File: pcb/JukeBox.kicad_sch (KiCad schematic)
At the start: 99 parts, among them J1 USB_C_Receptacle_USB2.0_16P, Q1 Q_NPN_BEC, SW1 SW_SPST, SW10 SW_SPST, SW11 SW_SPST, SW12 SW_SPST, SW2 SW_SPST, SW3 SW_SPST, SW4 SW_SPST, SW5 SW_SPST, SW6 SW_SPST, SW7 SW_SPST, SW8 SW_SPST, SW9 SW_SPST, U1 NCP1117-3.3_SOT223, U2 W25Q128JVS, U3 RP2350_60QFN, U5 CAT24C512, Y2 ABM8-272-T3

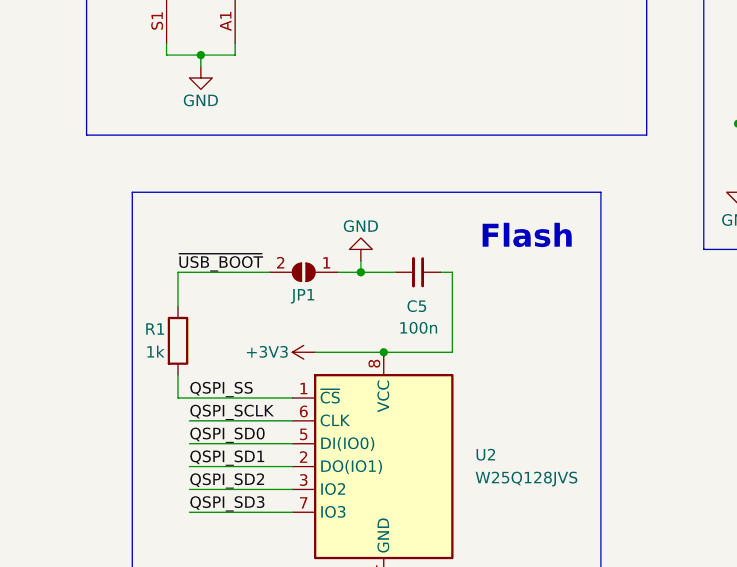
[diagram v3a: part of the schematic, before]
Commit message: add bootsel button instead of pad
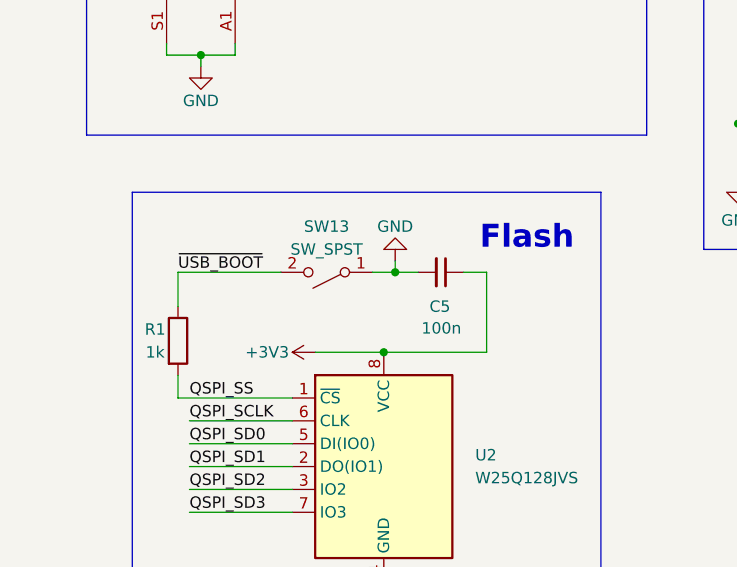
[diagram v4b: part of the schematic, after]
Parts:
- removed JP1: SolderJumper_2_Open, Jumper:SolderJumper-2_P1.3mm_Open_RoundedPad1.0x1.5mm, symbol Jumper:SolderJumper_2_Open
- added SW13: SW_SPST, Button_Switch_SMD:SW_SPST_CK_RS282G05A3, symbol Switch:SW_SPST
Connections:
- net GND: now also SW13.1 (A)
- net ~{USB_BOOT}: now also SW13.2 (B)
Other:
- moved on the sheet: C5
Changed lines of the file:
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@@
 	)
 	(junction
+		(at 58.42 99.06)
+		(diameter 0)
+		(color 0 0 0 0)
+	)
+	(junction
 		(at 111.76 82.55)
 		(diameter 0)
@@
 	)
 	(junction
-		(at 54.61 99.06)
-		(diameter 0)
-		(color 0 0 0 0)
-	)
-	(junction
 		(at 360.68 231.14)
 		(diameter 0)
@@
 	(wire
 		(pts
+			(xy 58.42 99.06) (xy 60.96 99.06)
+		)
+		(stroke
+			(width 0)
+			(type default)
+		)
+	)
+	(wire
+		(pts
 			(xy 203.2 157.48) (xy 203.2 158.75)
 		)
@@
 	(wire
 		(pts
-			(xy 57.15 107.95) (xy 64.77 107.95)
+			(xy 57.15 107.95) (xy 68.58 107.95)
 		)
 		(stroke
@@
 	(wire
 		(pts
-			(xy 63.5 99.06) (xy 64.77 99.06)
+			(xy 66.04 99.06) (xy 68.58 99.06)
 		)
 		(stroke
@@
 	(wire
 		(pts
-			(xy 54.61 97.79) (xy 54.61 99.06)
+			(xy 58.42 97.79) (xy 58.42 99.06)
+		)
+		(stroke
+			(width 0)
+			(type default)
+		)
+	)
+	(wire
+		(pts
+			(xy 55.88 99.06) (xy 58.42 99.06)
 		)
 		(stroke
@@
 	(wire
 		(pts
-			(xy 64.77 99.06) (xy 64.77 107.95)
+			(xy 68.58 99.06) (xy 68.58 107.95)
 		)
 		(stroke
@@
 	(wire
 		(pts
-			(xy 54.61 99.06) (xy 58.42 99.06)
-		)
-		(stroke
-			(width 0)
-			(type default)
-		)
-	)
-	(wire
-		(pts
 			(xy 173.99 157.48) (xy 171.45 157.48)
 		)
@@
 	(wire
 		(pts
-			(xy 34.29 99.06) (xy 44.45 99.06)
+			(xy 34.29 99.06) (xy 45.72 99.06)
 		)
 		(stroke
@@
 	(wire
 		(pts
-			(xy 52.07 99.06) (xy 54.61 99.06)
-		)
-		(stroke
-			(width 0)
-			(type default)
-		)
-	)
-	(wire
-		(pts
 			(xy 171.45 135.89) (xy 171.45 137.16)
 		)
@@
 	(symbol
 		(lib_id "Device:C_Small")
-		(at 60.96 99.06 270)
+		(at 63.5 99.06 270)
 		(unit 1)
 		(exclude_from_sim no)
@@
 		(dnp no)
 		(property "Reference" "C5"
-			(at 59.69 102.87 90)
+			(at 62.23 102.87 90)
 			(effects
 				(font
@@
 		)
 		(property "Value" "100n"
-			(at 58.801 105.283 90)
+			(at 61.341 105.283 90)
 			(effects
 				(font
@@
 		)
 		(property "Footprint" "Capacitor_SMD:C_0402_1005Metric"
-			(at 60.96 99.06 0)
+			(at 63.5 99.06 0)
 			(effects
 				(font
@@
 		)
 		(property "Datasheet" "~"
-			(at 60.96 99.06 0)
+			(at 63.5 99.06 0)
 			(effects
 				(font
@@
 		)
 		(property "Description" "Unpolarized capacitor, small symbol"
-			(at 60.96 99.06 0)
+			(at 63.5 99.06 0)
 			(effects
 				(font
@@
 	)
 	(symbol
-		(lib_id "Jumper:SolderJumper_2_Open")
-		(at 48.26 99.06 180)
-		(unit 1)
-		(exclude_from_sim no)
-		(in_bom yes)
-		(on_board yes)
-		(dnp no)
-		(property "Reference" "JP1"
-			(at 48.26 101.6 0)
-			(effects
-				(font
-					(size 1.27 1.27)
-				)
-			)
-		)
-		(property "Value" "SolderJumper_2_Open"
-			(at 48.26 104.14 0)
-			(effects
-				(font
-					(size 1.27 1.27)
-				)
-				(hide yes)
-			)
-		)
-		(property "Footprint" "Jumper:SolderJumper-2_P1.3mm_Open_RoundedPad1.0x1.5mm"
-			(at 48.26 99.06 0)
-			(effects
-				(font
-					(size 1.27 1.27)
-				)
-				(hide yes)
-			)
-		)
-		(property "Datasheet" "~"
-			(at 48.26 99.06 0)
-			(effects
-				(font
-					(size 1.27 1.27)
-				)
-				(hide yes)
-			)
-		)
-		(property "Description" ""
-			(at 48.26 99.06 0)
-			(effects
-				(font
-					(size 1.27 1.27)
-				)
-				(hide yes)
-			)
-		)
-		(pin "1"
-		)
-		(pin "2"
-		)
-		(instances
-			(project "JukeBox"
-				(path "/6328db6d-b3ae-4344-8bbe-195d6ec45eb3"
-					(reference "JP1")
-					(unit 1)
-				)
-			)
-		)
-	)
-	(symbol
 		(lib_id "Device:R")
 		(at 360.68 204.47 0)
@@
 	(symbol
 		(lib_id "power:GND")
-		(at 54.61 97.79 180)
+		(at 58.42 97.79 180)
 		(unit 1)
 		(exclude_from_sim no)
@@
 		(dnp no)
 		(property "Reference" "#PWR022"
-			(at 54.61 91.44 0)
+			(at 58.42 91.44 0)
 			(effects
 				(font
@@
 		)
 		(property "Value" "GND"
-			(at 54.61 93.98 0)
+			(at 58.42 93.98 0)
 			(effects
 				(font
@@
 		)
 		(property "Footprint" ""
-			(at 54.61 97.79 0)
+			(at 58.42 97.79 0)
 			(effects
 				(font
@@
 		)
 		(property "Datasheet" ""
-			(at 54.61 97.79 0)
+			(at 58.42 97.79 0)
 			(effects
 				(font
@@
 		)
 		(property "Description" ""
-			(at 54.61 97.79 0)
+			(at 58.42 97.79 0)
 			(effects
 				(font
@@
 					(unit 1)
 				)
+			)
+		)
+	)
+	(symbol
+		(lib_id "Switch:SW_SPST")
+		(at 50.8 99.06 180)
+		(unit 1)
+		(exclude_from_sim no)
+		(in_bom yes)
+		(on_board yes)
+		(dnp no)
+		(fields_autoplaced yes)
+		(property "Reference" "SW13"
+			(at 50.8 93.98 0)
+			(effects
+				(font
+					(size 1.27 1.27)
+				)
+			)
+		)
+		(property "Value" "SW_SPST"
+			(at 50.8 96.52 0)
+			(effects
+				(font
+					(size 1.27 1.27)
+				)
+			)
+		)
+		(property "Footprint" "Button_Switch_SMD:SW_SPST_CK_RS282G05A3"
+			(at 50.8 99.06 0)
+			(effects
+				(font
+					(size 1.27 1.27)
+				)
+				(hide yes)
+			)
+		)
+		(property "Datasheet" "~"
+			(at 50.8 99.06 0)
+			(effects
+				(font
+					(size 1.27 1.27)
+				)
+				(hide yes)
+			)
+		)
+		(property "Description" "Single Pole Single Throw (SPST) switch"
+			(at 50.8 99.06 0)
+			(effects
+				(font
+					(size 1.27 1.27)
+				)
+				(hide yes)
+			)
+		)
+		(pin "1"
+		)
+		(pin "2"
+		)
+		(instances
+			(project ""
+				(path "/6328db6d-b3ae-4344-8bbe-195d6ec45eb3"
+					(reference "SW13")
+					(unit 1)
+				)

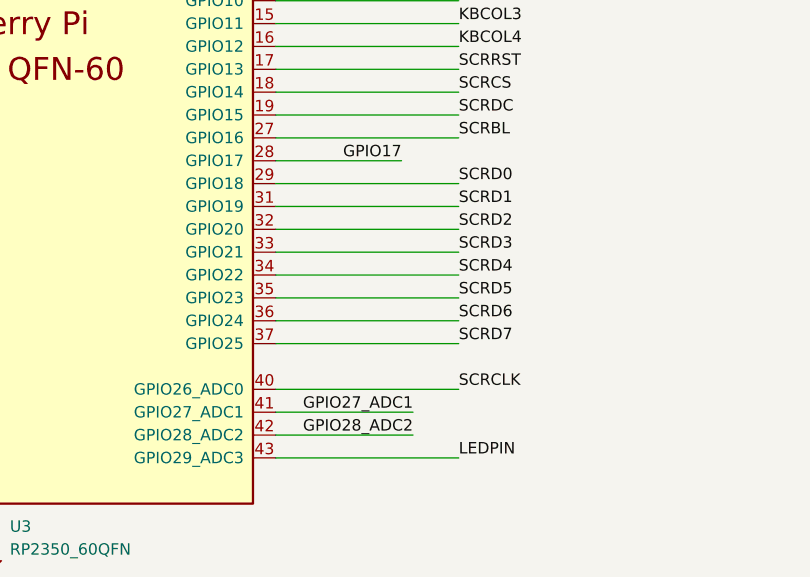
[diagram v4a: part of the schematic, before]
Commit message: finalize pinout and routing for screen, add models for missing components
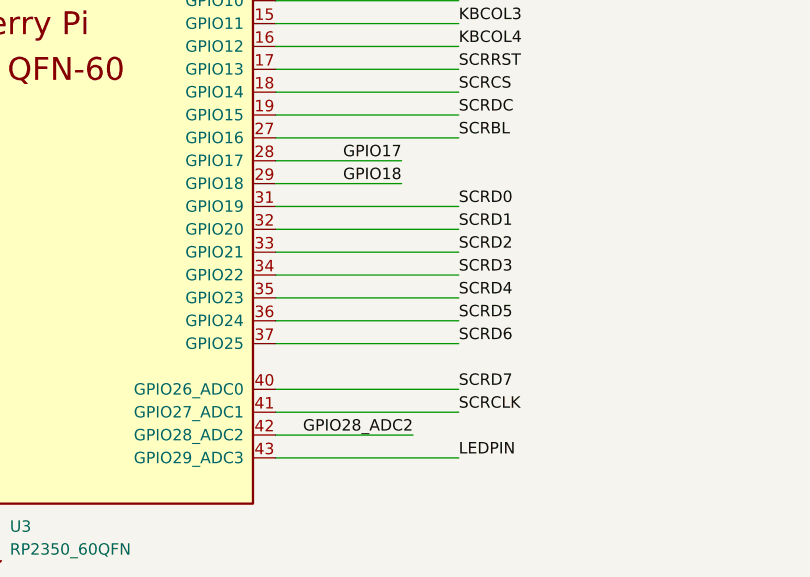
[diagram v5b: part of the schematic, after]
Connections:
- net GPIO27_ADC1 is gone; now on net SCRCLK: U3.41 (GPIO27_ADC1)
- net SCRCLK: no longer U3.40 (GPIO26_ADC0)
- net SCRD0: now also U3.31 (GPIO19); no longer U3.29 (GPIO18)
- net SCRD1: now also U3.32 (GPIO20); no longer U3.31 (GPIO19)
- net SCRD2: now also U3.33 (GPIO21); no longer U3.32 (GPIO20)
- net SCRD3: now also U3.34 (GPIO22); no longer U3.33 (GPIO21)
- net SCRD4: now also U3.35 (GPIO23); no longer U3.34 (GPIO22)
- net SCRD5: now also U3.36 (GPIO24); no longer U3.35 (GPIO23)
- net SCRD6: now also U3.37 (GPIO25); no longer U3.36 (GPIO24)
- net SCRD7: now also U3.40 (GPIO26_ADC0); no longer U3.37 (GPIO25)
- new net GPIO18: U3.29 (GPIO18)
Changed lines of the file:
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@@
 	(wire
 		(pts
+			(xy 226.06 245.11) (xy 246.38 245.11)
+		)
+		(stroke
+			(width 0)
+			(type default)
+		)
+	)
+	(wire
+		(pts
 			(xy 233.68 22.86) (xy 248.92 22.86)
 		)
@@
 	(wire
 		(pts
+			(xy 226.06 222.25) (xy 240.03 222.25)
+		)
+		(stroke
+			(width 0)
+			(type default)
+		)
+	)
+	(wire
+		(pts
 			(xy 55.88 196.85) (xy 55.88 194.31)
 		)
@@
 	(wire
 		(pts
-			(xy 226.06 222.25) (xy 246.38 222.25)
-		)
-		(stroke
-			(width 0)
-			(type default)
-		)
-	)
-	(wire
-		(pts
 			(xy 273.05 147.32) (xy 261.62 147.32)
 		)
@@
 	(wire
 		(pts
-			(xy 226.06 245.11) (xy 246.38 245.11)
-		)
-		(stroke
-			(width 0)
-			(type default)
-		)
-	)
-	(wire
-		(pts
 			(xy 55.88 40.64) (xy 69.85 40.64)
 		)
@@
 	(wire
 		(pts
-			(xy 226.06 247.65) (xy 241.3 247.65)
+			(xy 226.06 247.65) (xy 246.38 247.65)
 		)
 		(stroke
@@
 		)
 	)
-	(label "SCRD0"
-		(at 246.38 222.25 0)
+	(label "SCRD3"
+		(at 246.38 232.41 0)
 		(effects
 			(font
@@
 		)
 	)
-	(label "SCRD5"
-		(at 246.38 234.95 0)
+	(label "SCRD6"
+		(at 246.38 240.03 0)
 		(effects
 			(font
@@
 		)
 	)
-	(label "GPIO27_ADC1"
-		(at 241.3 247.65 180)
-		(effects
-			(font
-				(size 1.27 1.27)
-			)
-			(justify right bottom)
-		)
-	)
 	(label "DBGTX"
 		(at 34.29 194.31 180)
@@
 		)
 	)
-	(label "SCRD6"
-		(at 246.38 237.49 0)
+	(label "USB_D-"
+		(at 86.36 200.66 180)
 		(effects
 			(font
 				(size 1.27 1.27)
 			)
-			(justify left bottom)
+			(justify right bottom)
 		)
 	)
-	(label "USB_D-"
-		(at 86.36 200.66 180)
+	(label "SCRD4"
+		(at 246.38 234.95 0)
 		(effects
 			(font
 				(size 1.27 1.27)
 			)
-			(justify right bottom)
+			(justify left bottom)
 		)
 	)
@@
 		)
 	)
-	(label "SCRD7"
-		(at 246.38 240.03 0)
-		(effects
-			(font
-				(size 1.27 1.27)
-			)
-			(justify left bottom)
-		)
-	)
 	(label "DBGTX"
 		(at 246.38 179.07 0)
@@
 		)
 	)
+	(label "SCRD5"
+		(at 246.38 237.49 0)
+		(effects
+			(font
+				(size 1.27 1.27)
+			)
+			(justify left bottom)
+		)
+	)
 	(label "XOUT"
 		(at 151.13 217.17 0)
@@
 		)
 	)
+	(label "SCRD0"
+		(at 246.38 224.79 0)
+		(effects
+			(font
+				(size 1.27 1.27)
+			)
+			(justify left bottom)
+		)
+	)
 	(label "KBCOL4"
 		(at 246.38 207.01 0)
@@
 		)
 	)
-	(label "QSPI_SD3"
-		(at 151.13 199.39 0)
+	(label "SCRD7"
+		(at 246.38 245.11 0)
 		(effects
 			(font
@@
 		)
 	)
-	(label "SCRD3"
-		(at 246.38 229.87 0)
+	(label "QSPI_SD3"
+		(at 151.13 199.39 0)
 		(effects
 			(font
@@
 		)
 	)
-	(label "SCRCLK"
-		(at 246.38 245.11 0)
-		(effects
-			(font
-				(size 1.27 1.27)
-			)
-			(justify left bottom)
-		)
-	)
 	(label "KBCOL1"
 		(at 246.38 199.39 0)
@@
 		)
 	)
-	(label "SCRD4"
-		(at 246.38 232.41 0)
-		(effects
-			(font
-				(size 1.27 1.27)
-			)
-			(justify left bottom)
-		)
-	)
 	(label "QSPI_SS"
 		(at 35.56 113.03 0)
@@
 		)
 	)
-	(label "SCRD2"
-		(at 246.38 227.33 0)
-		(effects
-			(font
-				(size 1.27 1.27)
-			)
-			(justify left bottom)
-		)
-	)
 	(label "SCRRST"
 		(at 351.79 90.17 180)
@@
 		)
 	)
+	(label "GPIO18"
+		(at 240.03 222.25 180)
+		(effects
+			(font
+				(size 1.27 1.27)
+			)
+			(justify right bottom)
+		)
+	)
+	(label "SCRD2"
+		(at 246.38 229.87 0)
+		(effects
+			(font
+				(size 1.27 1.27)
+			)
+			(justify left bottom)
+		)
+	)
 	(label "QSPI_SD2"
 		(at 151.13 196.85 0)
@@
 		)
 	)
+	(label "SCRD1"
+		(at 246.38 227.33 0)
+		(effects
+			(font
+				(size 1.27 1.27)
+			)
+			(justify left bottom)
+		)
+	)
 	(label "USB_D+"
 		(at 255.27 160.02 180)
@@
 		)
 	)
+	(label "SCRCLK"
+		(at 246.38 247.65 0)
+		(effects
+			(font
+				(size 1.27 1.27)
+			)
+			(justify left bottom)
+		)
+	)
 	(label "DBGRX"
 		(at 34.29 199.39 180)
@@
 		(effects
 			(font
-				(size 1.27 1.27)
-			)
-			(justify left bottom)
-		)
-	)
-	(label "SCRD1"
-		(at 246.38 224.79 0)
-		(effects
-			(font

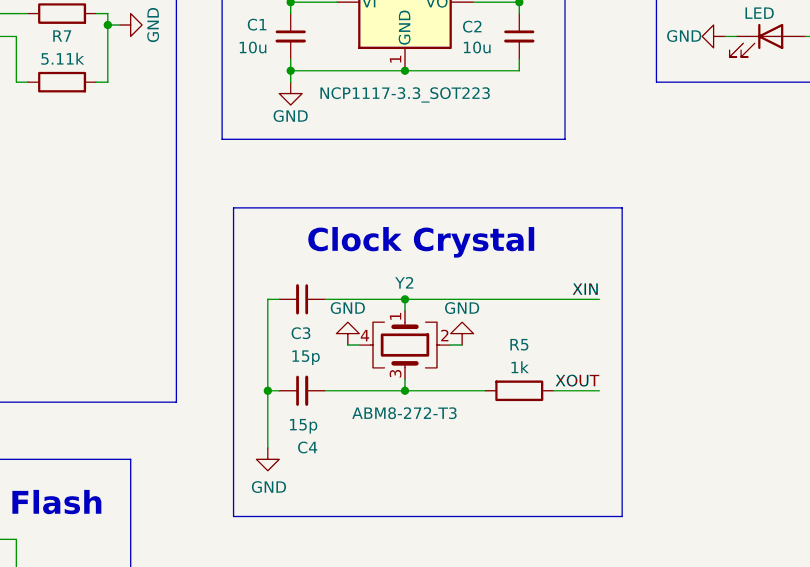
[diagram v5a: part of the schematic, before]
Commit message: fix designator for clock crystal
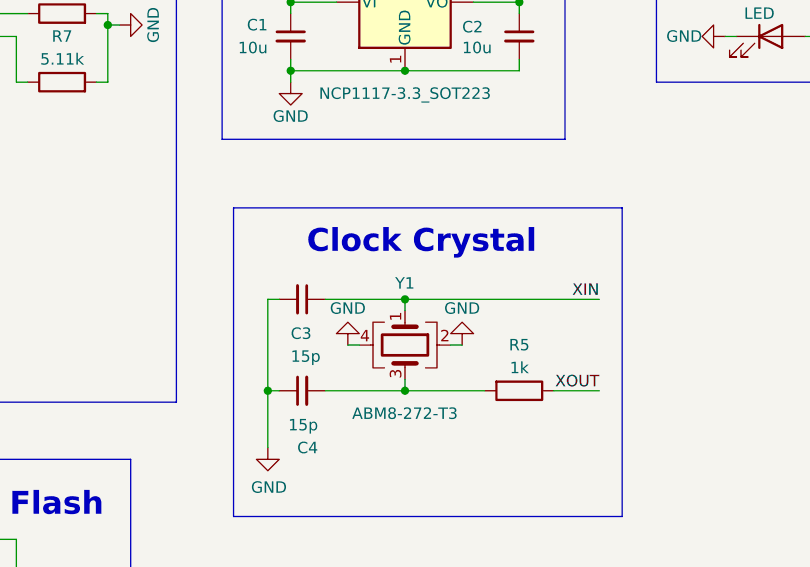
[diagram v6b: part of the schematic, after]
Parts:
- renumbered Y2 to Y1
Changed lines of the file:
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@@
 		(on_board yes)
 		(dnp no)
-		(property "Reference" "Y2"
+		(property "Reference" "Y1"
 			(at 111.76 70.612 90)
 			(effects
@@
 			(project ""
 				(path "/6328db6d-b3ae-4344-8bbe-195d6ec45eb3"
-					(reference "Y2")
+					(reference "Y1")
 					(unit 1)
 				)

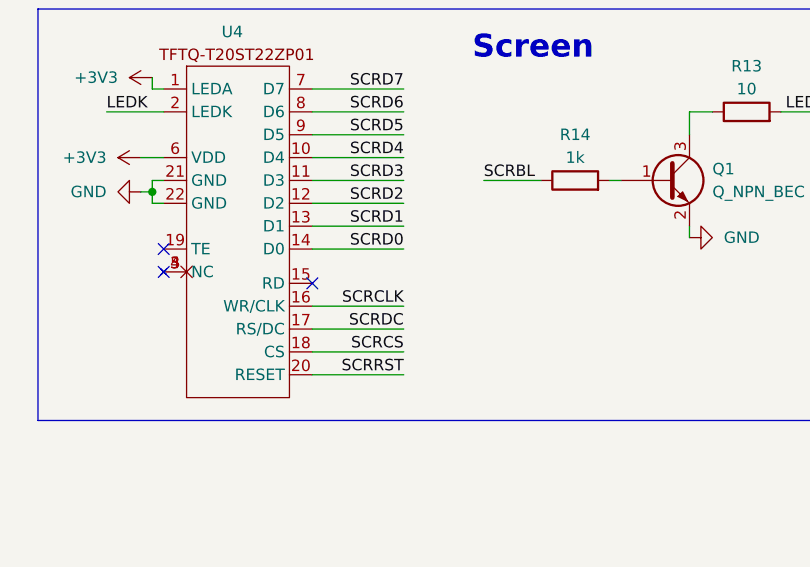
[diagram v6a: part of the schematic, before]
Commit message: fix floating read clock on screen, which causes the screen to hang on startup
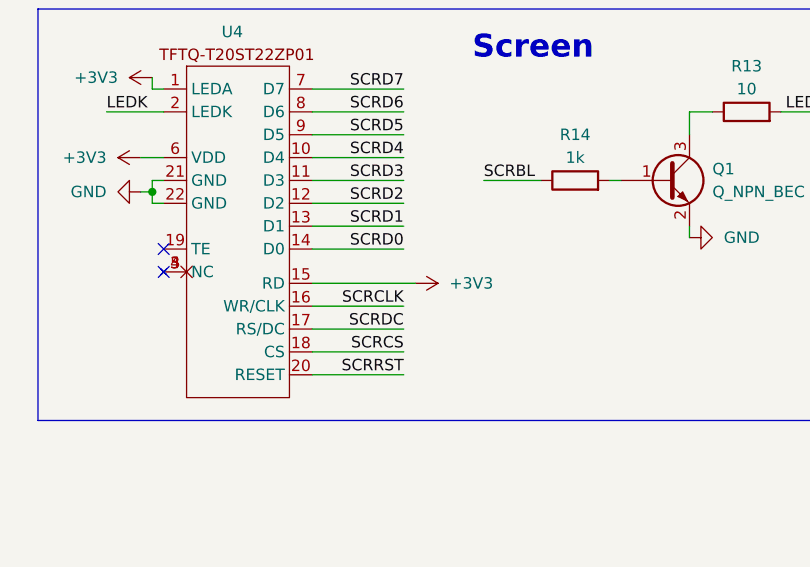
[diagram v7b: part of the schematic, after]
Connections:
- net +3V3: now also U4.15 (RD)
- no-connect marks 5 -> 4
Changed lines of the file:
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@@
 	)
 	(no_connect
-		(at 341.63 80.01)
-	)
-	(no_connect
 		(at 55.88 66.04)
 	)
@@
 	(wire
 		(pts
+			(xy 341.63 80.01) (xy 353.06 80.01)
+		)
+		(stroke
+			(width 0)
+			(type default)
+		)
+	)
+	(wire
+		(pts
 			(xy 124.46 39.37) (xy 124.46 40.64)
 		)
@@
 					(unit 1)
 				)
+			)
+		)
+	)
+	(symbol
+		(lib_id "power:+3V3")
+		(at 353.06 80.01 270)
+		(unit 1)
+		(exclude_from_sim no)
+		(in_bom yes)
+		(on_board yes)
+		(dnp no)
+		(fields_autoplaced yes)
+		(property "Reference" "#PWR16"
+			(at 349.25 80.01 0)
+			(effects
+				(font
+					(size 1.27 1.27)
+				)
+				(hide yes)
+			)
+		)
+		(property "Value" "+3V3"
+			(at 356.87 80.0099 90)
+			(effects
+				(font
+					(size 1.27 1.27)
+				)
+				(justify left)
+			)
+		)
+		(property "Footprint" ""
+			(at 353.06 80.01 0)
+			(effects
+				(font
+					(size 1.27 1.27)
+				)
+				(hide yes)
+			)
+		)
+		(property "Datasheet" ""
+			(at 353.06 80.01 0)
+			(effects
+				(font
+					(size 1.27 1.27)
+				)
+				(hide yes)
+			)
+		)
+		(property "Description" ""
+			(at 353.06 80.01 0)
+			(effects
+				(font
+					(size 1.27 1.27)
+				)
+				(hide yes)
+			)
+		)
+		(pin "1"
+		)
+		(instances
+			(project "JukeBox"
+				(path "/6328db6d-b3ae-4344-8bbe-195d6ec45eb3"
+					(reference "#PWR16")
+					(unit 1)
+				)
